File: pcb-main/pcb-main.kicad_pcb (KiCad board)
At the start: 2 copper layers, 86 x 86 mm, 37 parts, among them J1 AVR-ISP-6, J2 Conn_02x06_Counter_Clockwise, M1 Stepper_Motor, SW1 SW_MEC_5E, SW2 SW_MEC_5E, U1 ATmega328P-AU, U2 HT1621B-LQFP-A, U3 VIM878, U4 PCF8563T, Y1 16MHz, Y2 32kHz

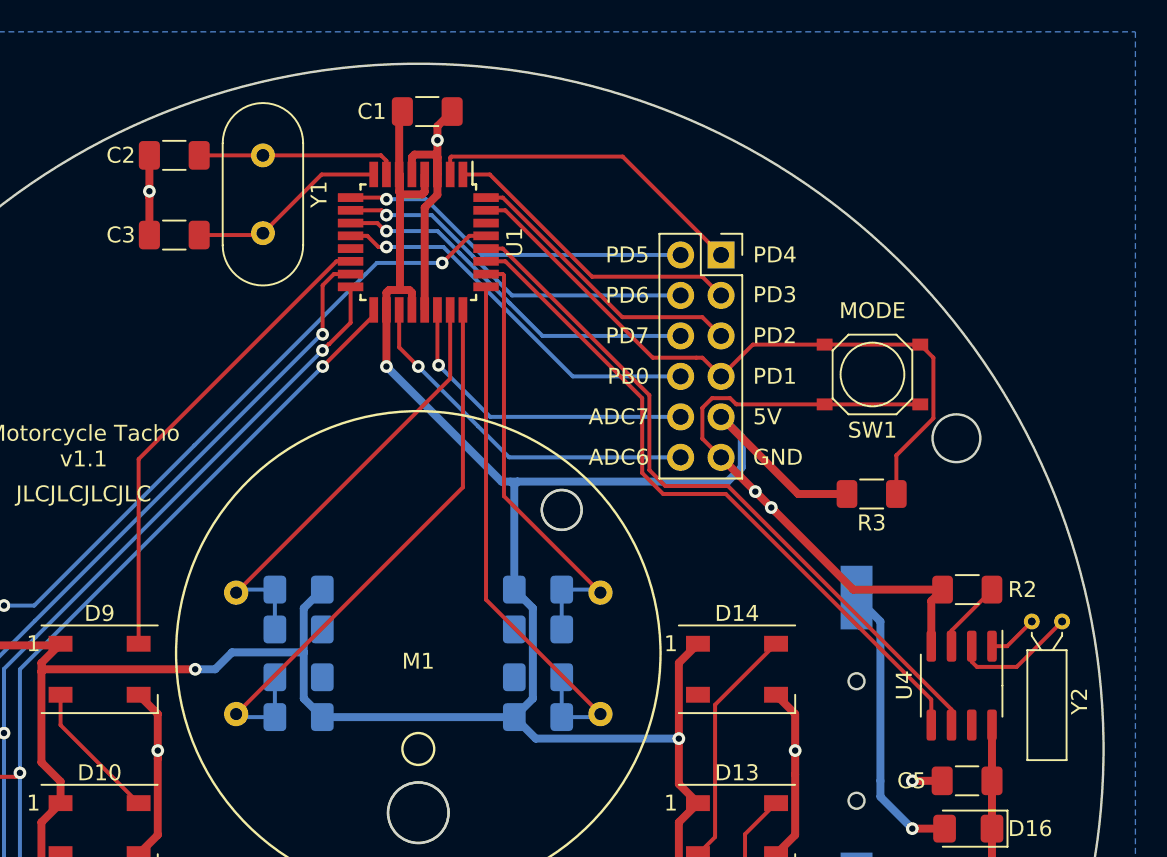
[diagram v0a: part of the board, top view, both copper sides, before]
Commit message: resolves #39: smd crystals
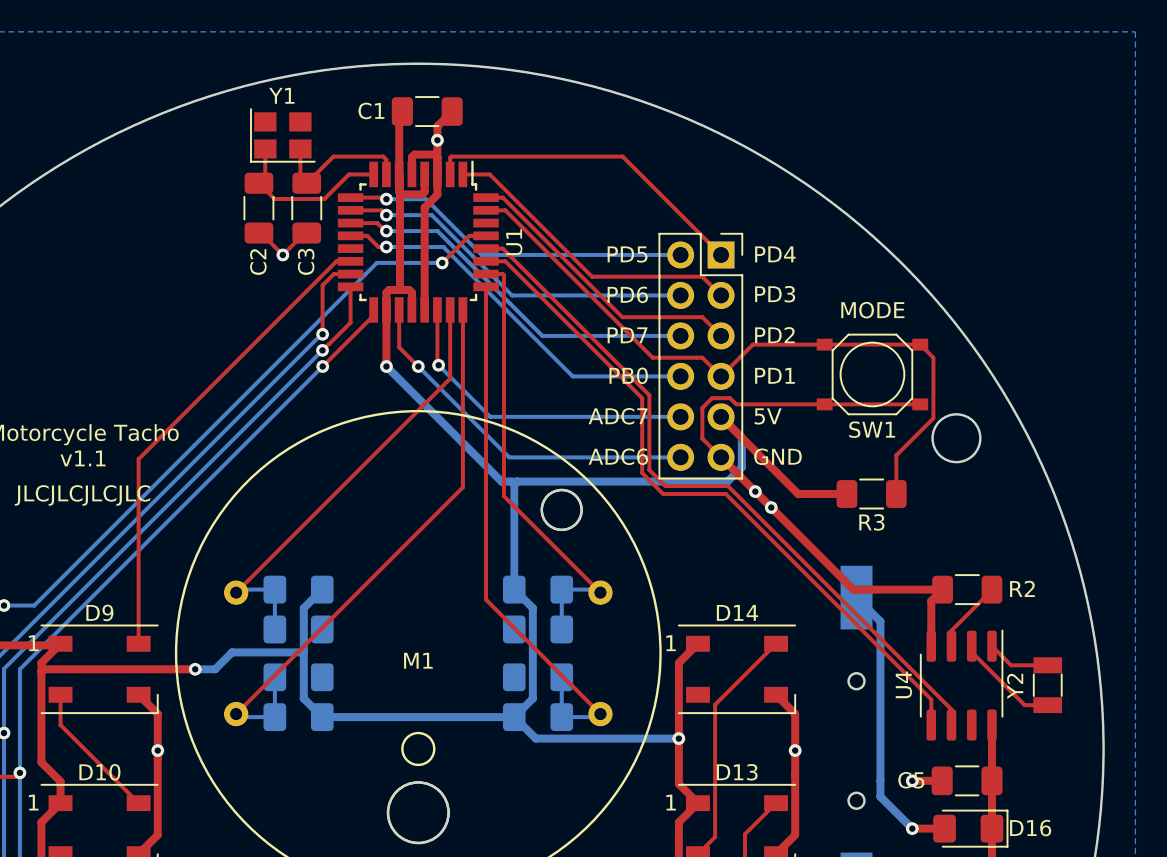
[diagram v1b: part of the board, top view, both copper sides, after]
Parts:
- Y1: footprint Crystal:Crystal_HC49-4H_Vertical -> Crystal:Crystal_SMD_3225-4Pin_3.2x2.5mm
- Y2: footprint Crystal:Crystal_C26-LF_D2.1mm_L6.5mm_Horizontal -> Crystal:Crystal_SMD_3215-2Pin_3.2x1.5mm
- moved C3 8.48 mm to (143.0, 66.1), turned to -90 degrees
- moved C2 6.26 mm to (140.0, 66.1), turned to 90 degrees
- moved Y2 4.12 mm to (189.5, 96.0), turned to 90 degrees
- moved Y1 1.77 mm to (141.5, 61.5), turned to 0 degrees
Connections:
- C2 pad 1: /XTAL1 -> GND
- C2 pad 2: GND -> /XTAL2
- C3 pad 1: /XTAL2 -> /XTAL1
- Y1 pad 1: /XTAL1 -> /XTAL2
- Y1 pad 2: /XTAL2 -> /XTAL1
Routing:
- net /XTAL1: track 12.8 -> 9.02 mm
- net /XTAL2: track 12.5 -> 10.6 mm
- net Net-(U4-Pad2): track 7.96 -> 6.52 mm
- net GND: track 109.5 -> 108.7 mm
- net Net-(U4-Pad1): track 3.14 -> 4.00 mm

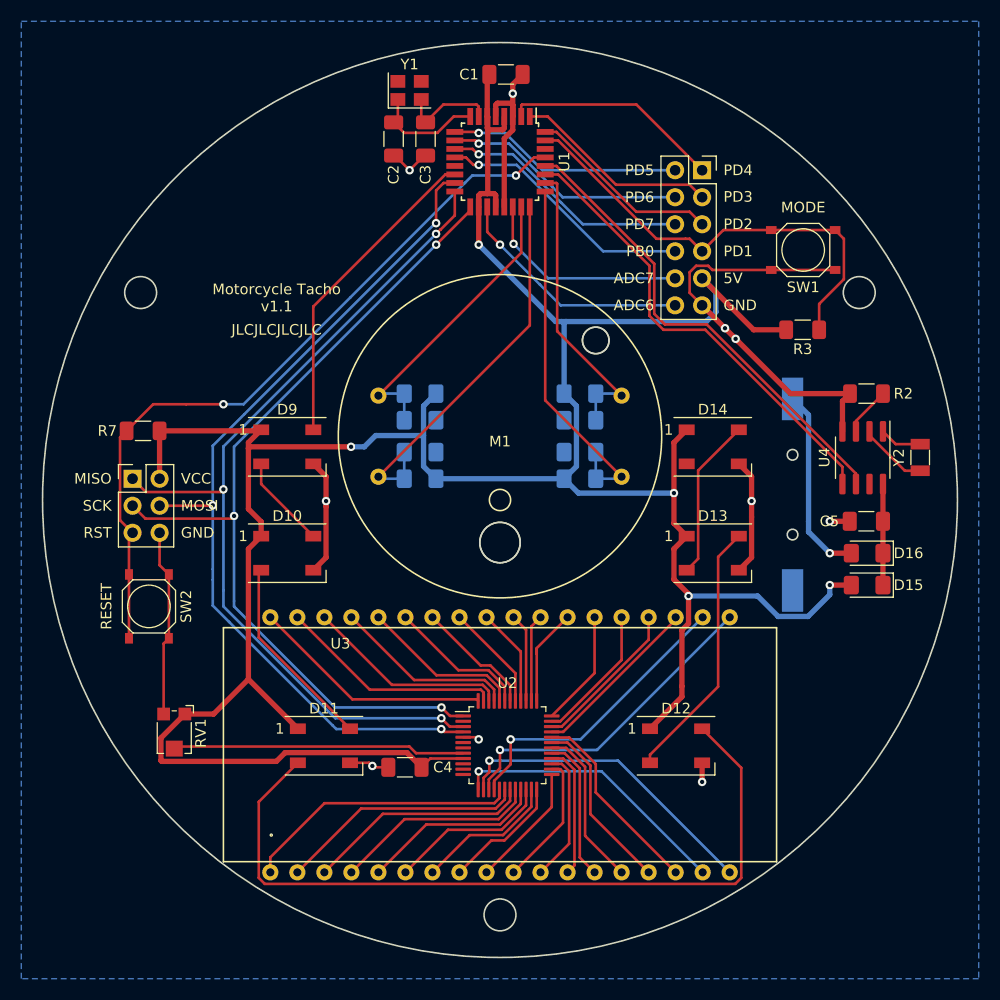
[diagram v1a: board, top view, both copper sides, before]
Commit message: resolves #18: integrated mode button
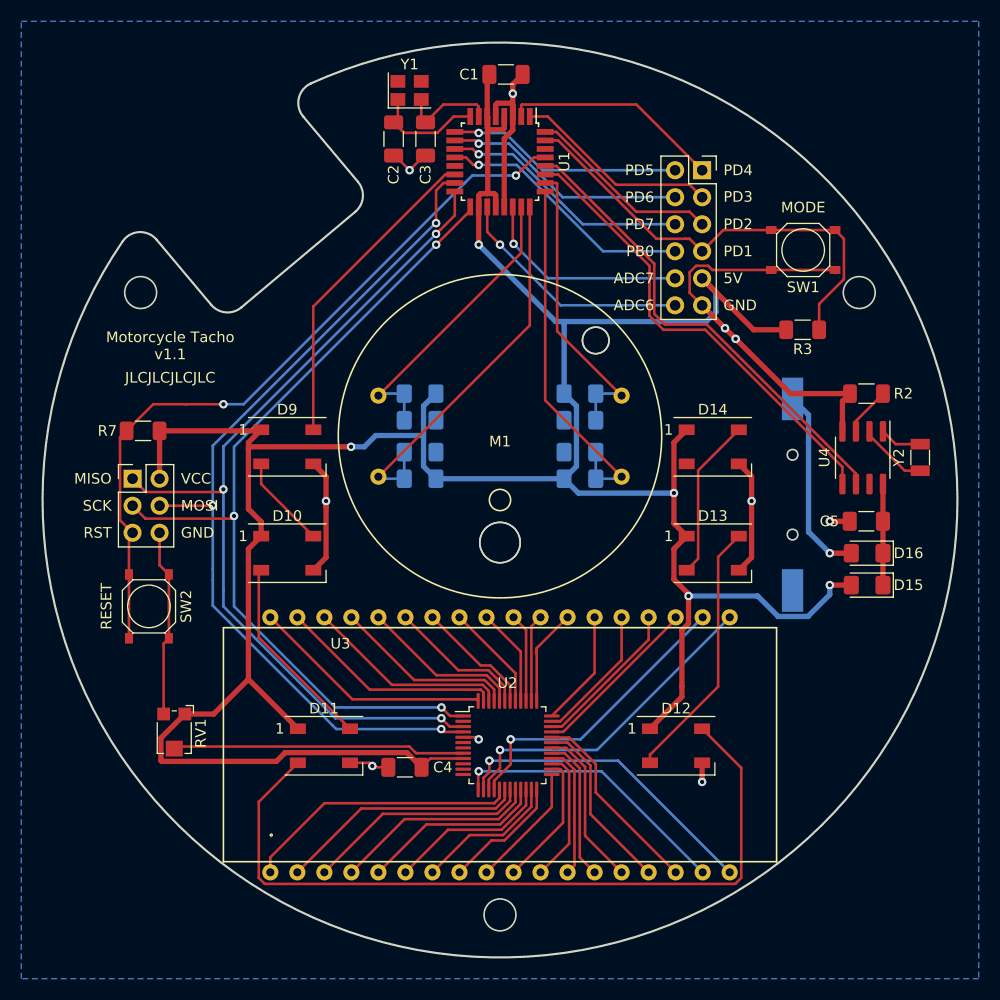
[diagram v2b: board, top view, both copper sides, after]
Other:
- outline, holes or cut-outs redrawn
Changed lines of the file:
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@@
       (net 2 "GND") (pinfunction "-") (pintype "passive"))
   )
-  (gr_circle (center 150 100) (end 193 100) (layer "Edge.Cuts") (width 0.15) (fill none))
+  (gr_arc (start 132.211225 60.852082) (mid 177.639867 132.939911) (end 114.535815 75.683512) (layer "Edge.Cuts") (width 0.2))
+  (gr_line (start 117.7175 75.5288) (end 122.8598 81.6571) (layer "Edge.Cuts") (width 0.2))
   (gr_circle (center 177.5 95.75) (end 178 95.75) (layer "Edge.Cuts") (width 0.15) (fill none))
+  (gr_arc (start 136.648589 70.086925) (mid 137.108889 71.546812) (end 136.402075 72.904589) (layer "Edge.Cuts") (width 0.2))
+  (gr_arc (start 131.506311 63.958575) (mid 131.087958 62.230533) (end 132.211015 60.852167) (layer "Edge.Cuts") (width 0.2))
+  (gr_line (start 136.6486 70.0869) (end 131.5063 63.9586) (layer "Edge.Cuts") (width 0.2))
   (gr_circle (center 150 139) (end 151.5 139) (layer "Edge.Cuts") (width 0.15) (fill none))
   (gr_circle (center 116.22 80.5) (end 117.72 80.5) (layer "Edge.Cuts") (width 0.15) (fill none))
   (gr_circle (center 159 85) (end 160.25 85) (layer "Edge.Cuts") (width 0.15) (fill none))
+  (gr_arc (start 125.677475 81.903589) (mid 124.217588 82.363889) (end 122.859811 81.657075) (layer "Edge.Cuts") (width 0.2))
+  (gr_arc (start 114.535903 75.683301) (mid 116.088345 74.816656) (end 117.717489 75.528725) (layer "Edge.Cuts") (width 0.2))
+  (gr_line (start 136.4021 72.9046) (end 125.6775 81.9036) (layer "Edge.Cuts") (width 0.2))
   (gr_circle (center 150 104) (end 151.9 104) (layer "Edge.Cuts") (width 0.15) (fill none))
   (gr_circle (center 177.5 103.25) (end 178 103.25) (layer "Edge.Cuts") (width 0.15) (fill none))
@@
     (effects (font (size 1 1) (thickness 0.15)) (justify right))
   )
-  (gr_text "Motorcycle Tacho\nv1.1" (at 129 81) (layer "F.SilkS")
+  (gr_text "Motorcycle Tacho\nv1.1" (at 119 85.5) (layer "F.SilkS")
     (effects (font (size 1 1) (thickness 0.15)))
   )
@@
     (effects (font (size 1 1) (thickness 0.15)) (justify right))
   )
-  (gr_text "JLCJLCJLCJLC" (at 129 84) (layer "F.SilkS")
+  (gr_text "JLCJLCJLCJLC" (at 119 88.5) (layer "F.SilkS")
     (effects (font (size 1 1) (thickness 0.15)))
   )
@@
     )
   )
+  (group "" (id 7c8f8bc3-a9ba-48f9-95d8-8c2f72134f34)
+    (members
+      06593c7a-eb1e-4af8-a146-199308d87368
+      0d59cf8c-90f1-4d94-8a3f-9000b6db27d4
+      2960c41e-c815-4702-8365-0e3f52b4cfab
+      52a612af-478b-4fd6-94e2-dd9838e1d253
+      6abb4ad3-39d9-41c2-b5ec-4d3074294147
+      94ae0783-fc18-464d-b820-64ee89d63c79
+      a6685c35-66bc-4082-aa2f-db0bd8b7309f
+      b4f7cc32-a8f5-4d4f-be1a-fffe887626df
+    )
+  )

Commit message: resolves #26: protection diodes
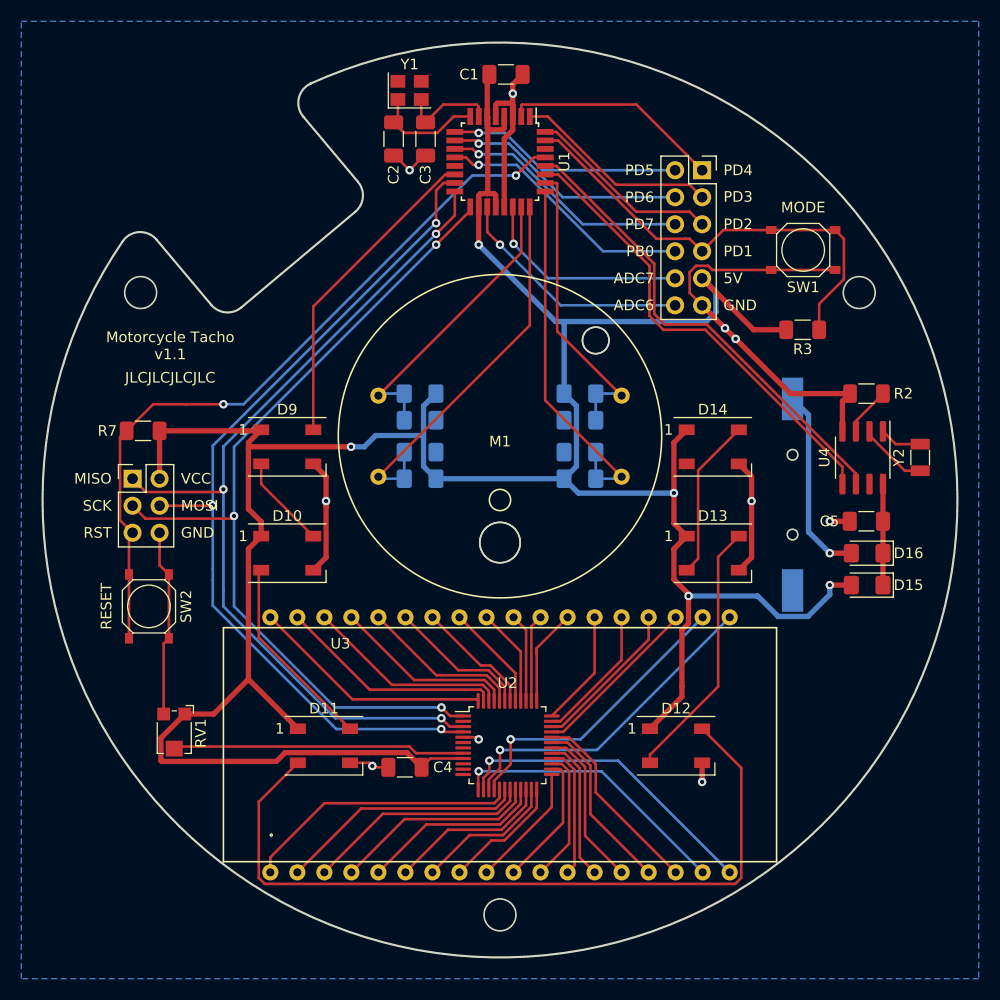
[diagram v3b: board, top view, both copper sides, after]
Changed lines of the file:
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@@
       (net 2 "GND") (pinfunction "-") (pintype "passive"))
   )
-  (gr_arc (start 132.211225 60.852082) (mid 177.639867 132.939911) (end 114.535815 75.683512) (layer "Edge.Cuts") (width 0.2))
-  (gr_line (start 117.7175 75.5288) (end 122.8598 81.6571) (layer "Edge.Cuts") (width 0.2))
+  (gr_arc (start 136.648625 70.086936) (mid 137.108925 71.546823) (end 136.402111 72.9046) (layer "Edge.Cuts") (width 0.2))
+  (gr_line (start 122.859825 81.657113) (end 117.717524 75.528757) (layer "Edge.Cuts") (width 0.2))
   (gr_circle (center 177.5 95.75) (end 178 95.75) (layer "Edge.Cuts") (width 0.15) (fill none))
-  (gr_arc (start 136.648589 70.086925) (mid 137.108889 71.546812) (end 136.402075 72.904589) (layer "Edge.Cuts") (width 0.2))
-  (gr_arc (start 131.506311 63.958575) (mid 131.087958 62.230533) (end 132.211015 60.852167) (layer "Edge.Cuts") (width 0.2))
-  (gr_line (start 136.6486 70.0869) (end 131.5063 63.9586) (layer "Edge.Cuts") (width 0.2))
+  (gr_arc (start 114.535944 75.683324) (mid 116.088386 74.816689) (end 117.717524 75.528757) (layer "Edge.Cuts") (width 0.2))
   (gr_circle (center 150 139) (end 151.5 139) (layer "Edge.Cuts") (width 0.15) (fill none))
+  (gr_line (start 136.402111 72.9046) (end 125.677489 81.903626) (layer "Edge.Cuts") (width 0.2))
   (gr_circle (center 116.22 80.5) (end 117.72 80.5) (layer "Edge.Cuts") (width 0.15) (fill none))
+  (gr_arc (start 132.211018 60.852176) (mid 177.639867 132.939911) (end 114.535944 75.683324) (layer "Edge.Cuts") (width 0.2))
   (gr_circle (center 159 85) (end 160.25 85) (layer "Edge.Cuts") (width 0.15) (fill none))
-  (gr_arc (start 125.677475 81.903589) (mid 124.217588 82.363889) (end 122.859811 81.657075) (layer "Edge.Cuts") (width 0.2))
-  (gr_arc (start 114.535903 75.683301) (mid 116.088345 74.816656) (end 117.717489 75.528725) (layer "Edge.Cuts") (width 0.2))
-  (gr_line (start 136.4021 72.9046) (end 125.6775 81.9036) (layer "Edge.Cuts") (width 0.2))
   (gr_circle (center 150 104) (end 151.9 104) (layer "Edge.Cuts") (width 0.15) (fill none))
   (gr_circle (center 177.5 103.25) (end 178 103.25) (layer "Edge.Cuts") (width 0.15) (fill none))
+  (gr_line (start 131.506324 63.95858) (end 136.648625 70.086936) (layer "Edge.Cuts") (width 0.2))
+  (gr_arc (start 125.677489 81.903626) (mid 124.217602 82.363927) (end 122.859825 81.657113) (layer "Edge.Cuts") (width 0.2))
+  (gr_arc (start 131.506324 63.95858) (mid 131.08797 62.230543) (end 132.211018 60.852176) (layer "Edge.Cuts") (width 0.2))
   (gr_circle (center 183.77 80.5) (end 185.27 80.5) (layer "Edge.Cuts") (width 0.15) (fill none))
   (gr_text "PD1" (at 171 76.62) (layer "F.SilkS")
@@
     )
   )
-  (group "" (id 7c8f8bc3-a9ba-48f9-95d8-8c2f72134f34)
+  (group "" (id dacf9367-b601-49bc-9028-b16153d0c0e9)
     (members
-      06593c7a-eb1e-4af8-a146-199308d87368
-      0d59cf8c-90f1-4d94-8a3f-9000b6db27d4
-      2960c41e-c815-4702-8365-0e3f52b4cfab
-      52a612af-478b-4fd6-94e2-dd9838e1d253
-      6abb4ad3-39d9-41c2-b5ec-4d3074294147
-      94ae0783-fc18-464d-b820-64ee89d63c79
-      a6685c35-66bc-4082-aa2f-db0bd8b7309f
-      b4f7cc32-a8f5-4d4f-be1a-fffe887626df
+      09836efc-c91d-45ee-86b9-df70c8da399e
+      20084455-918d-48d6-b766-f4767a31b475
+      5f03d484-e72e-4eb3-b5f7-0e8af7db7445
+      771107c7-339c-4b0b-9429-6daa4f7f1deb
+      82c9f256-c309-4d41-8731-04731f7a79cb
+      e0bdc109-f0e8-47f6-960d-f6a695b59a1c
+      e27ec783-dd3a-42a5-a750-16e001e401a9
+      eea71331-83eb-4182-b53f-416f25fbf23c
     )
   )

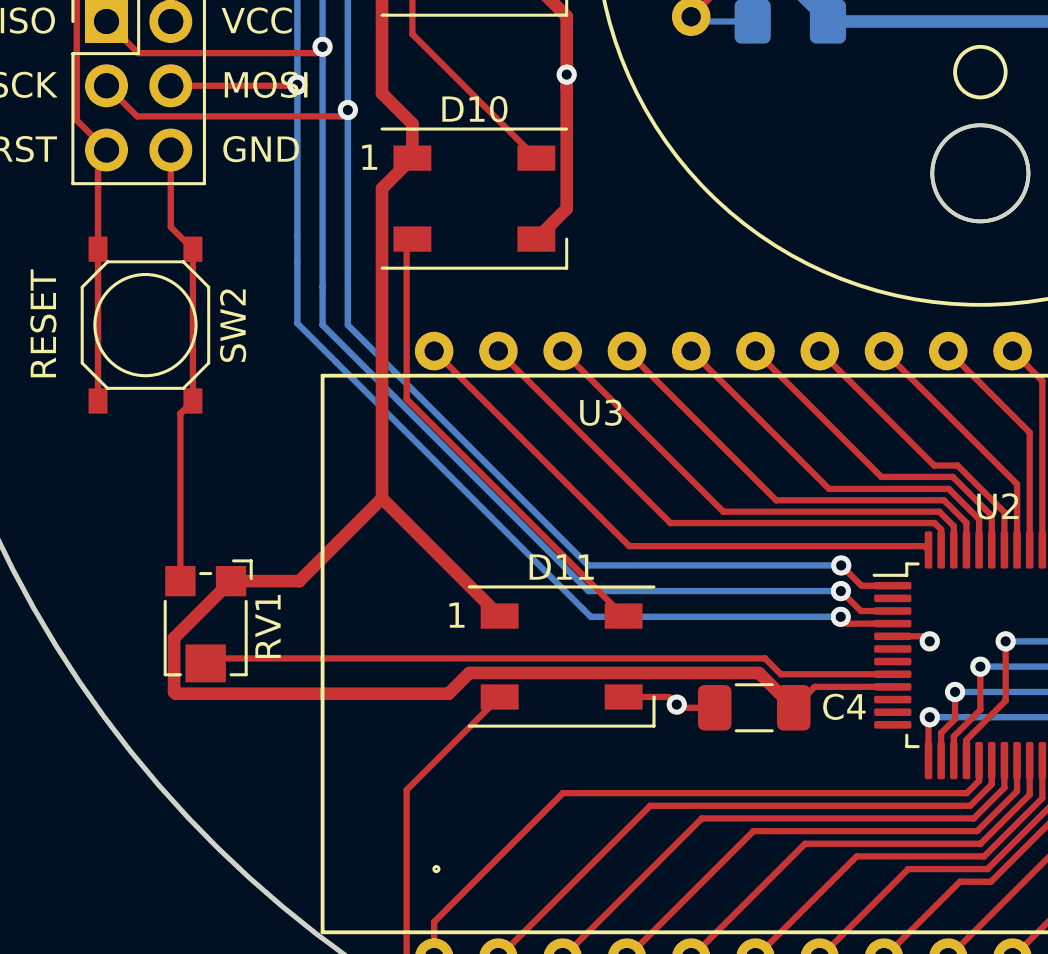
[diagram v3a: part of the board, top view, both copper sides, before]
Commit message: changed pot
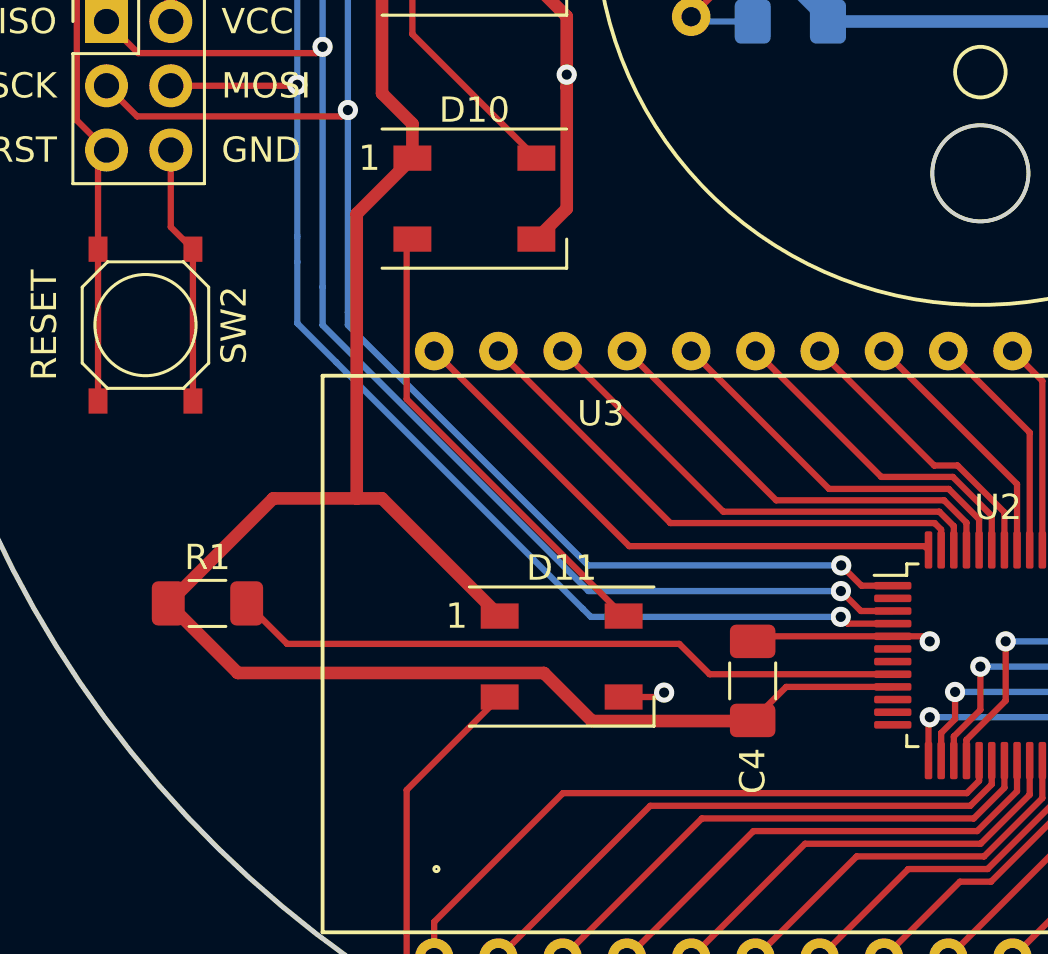
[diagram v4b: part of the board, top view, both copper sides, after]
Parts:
- removed RV1: 20k, Potentiometer_SMD:Potentiometer_Bourns_TC33X_Vertical
- added R1: 10k, Resistor_SMD:R_1206_3216Metric_Pad1.30x1.75mm_HandSolder, F.Cu at (119.5, 121.0)
- moved C4 1.06 mm to (141.0, 124.1), turned to 90 degrees
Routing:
- net GND: track 108.7 -> 104.9 mm
- net Net-(U2-Pad8): track 27.5 -> 26.7 mm
- net +5V: track 264.1 -> 263.5 mm
